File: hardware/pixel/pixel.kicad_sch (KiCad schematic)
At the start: 13 parts, among them J1 IN (male), J2 OUT (female), U1 WS2814F

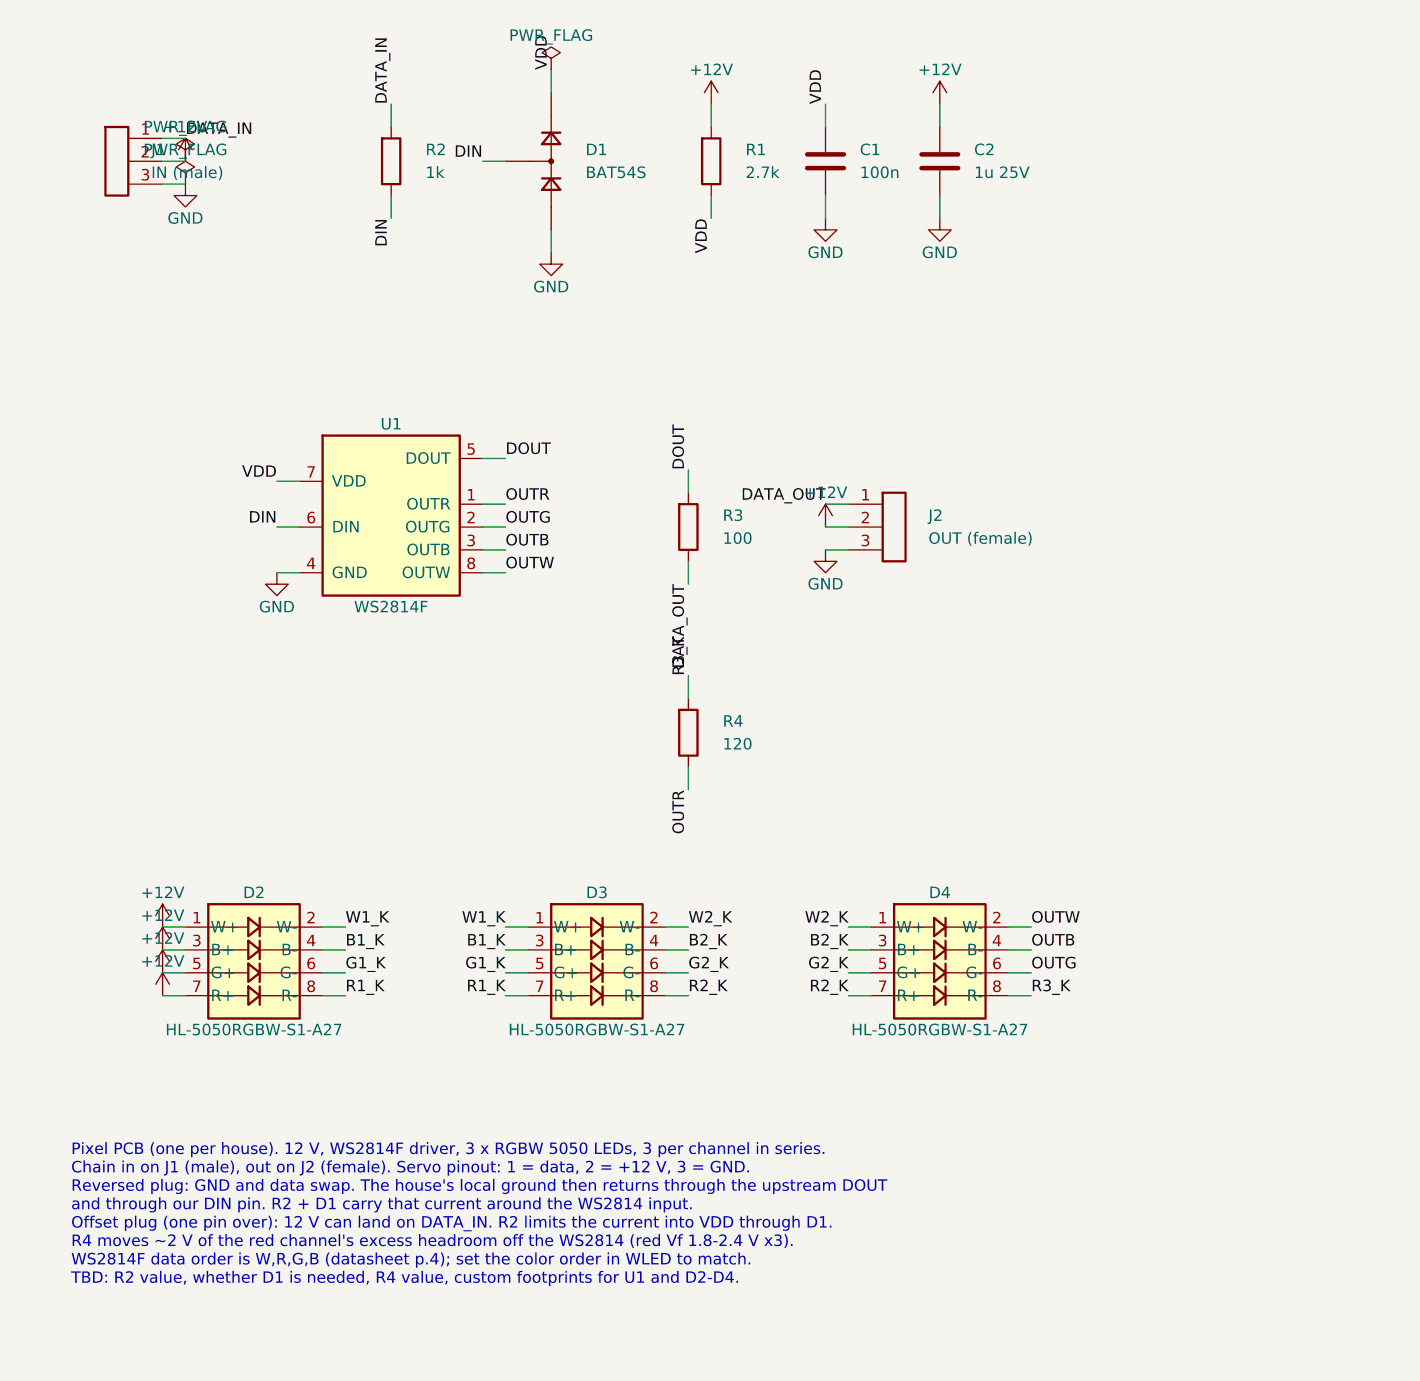
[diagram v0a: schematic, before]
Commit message: Pixel schematic: fix KiCad load error, use stock symbols, tidy layout
- Escape newlines in the notes text; KiCad 9.0.2 refused to load the file.
- Copy Device/Connector/power symbols verbatim from KiCad's stock libraries.
- Leave U1/LED footprints blank until the custom footprints exist.
- Rotate power symbols along their stubs, give PWR_FLAGs their own group,
  and space parts so labels don't overlap.

ERC in KiCad 9.0.2: 0 errors, 0 warnings. The kicad-cli netlist matches
the intended connectivity (20 nets).

Co-Authored-By: Claude Opus 5.5 <noreply@anthropic.com>
Claude-Session: https://claude.ai/code/session_01VgDz1r9wRYGVXFnVgHwR28
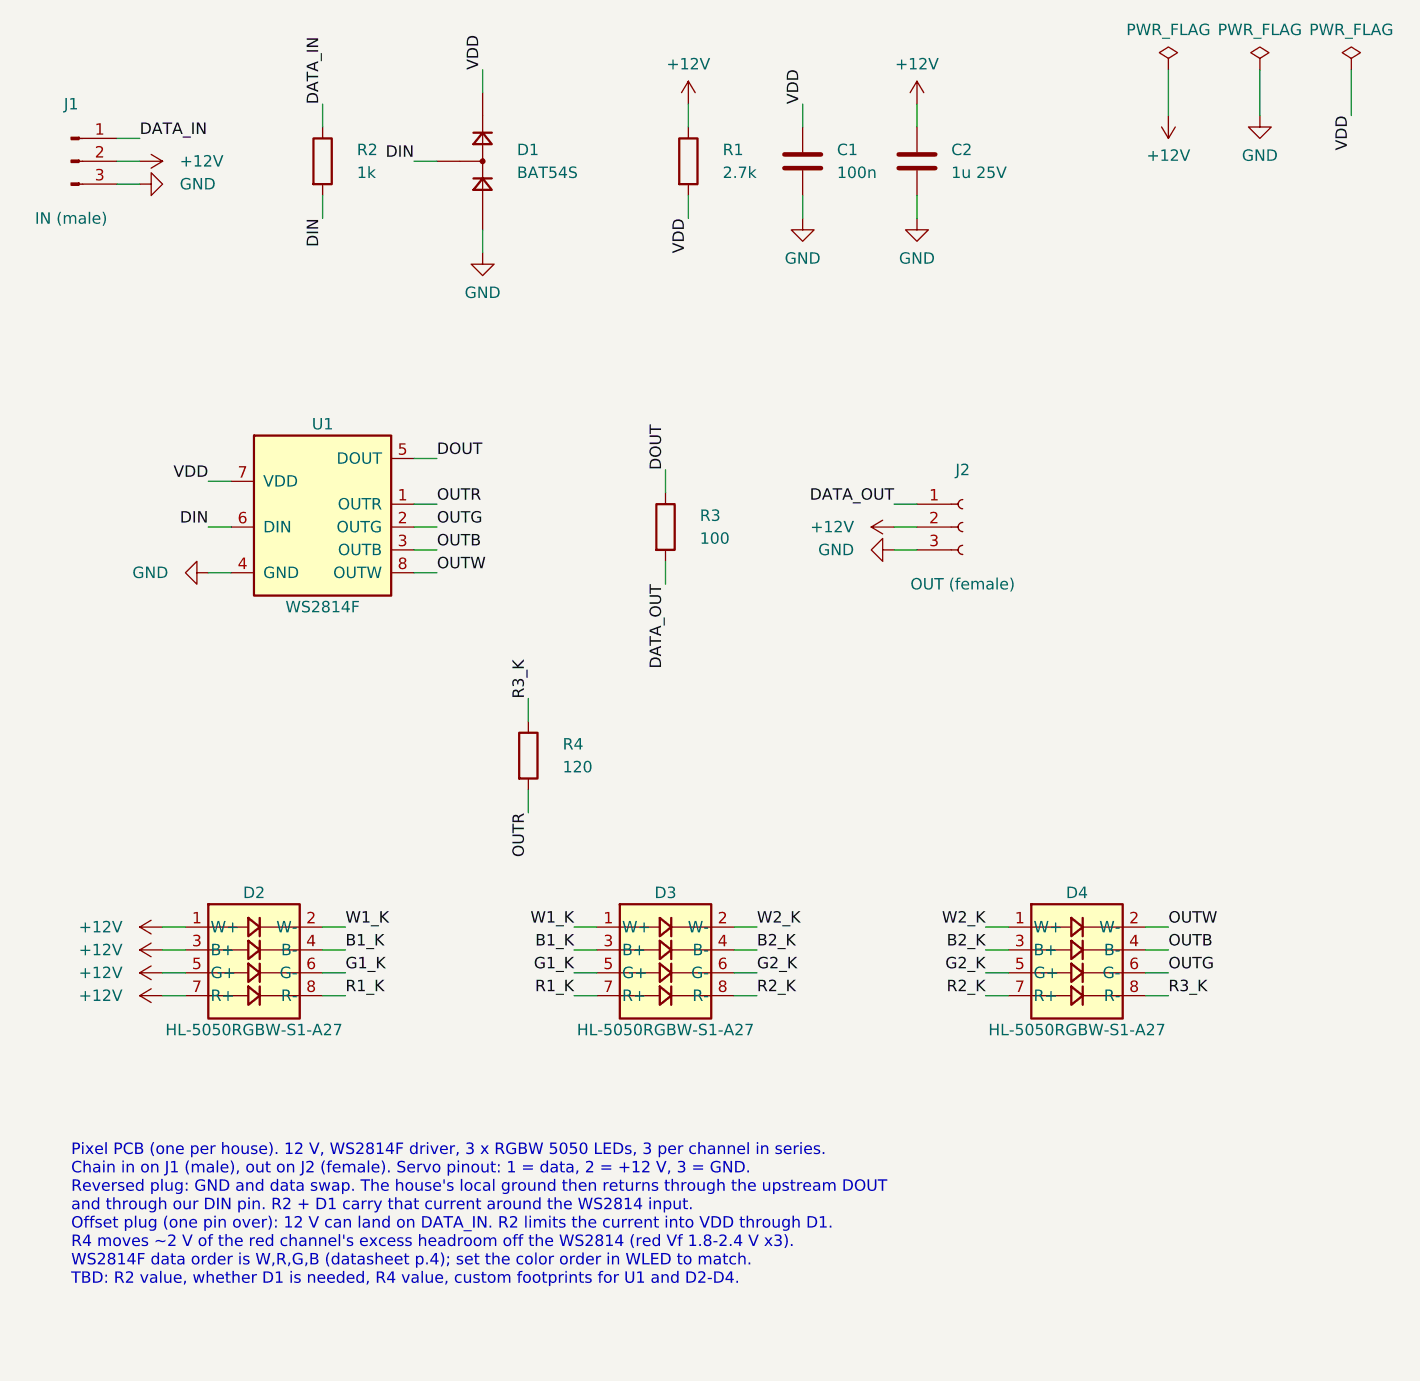
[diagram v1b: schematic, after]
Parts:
- D2, D3, D4: footprint village:LED_RGBW_5050-8P_HL -> (none)
- U1: footprint village:FSOP-8_2.85x3.25mm_P0.8mm -> (none)
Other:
- moved on the sheet: C1, C2, D1, D3, D4, R1, R2, R3, R4, U1

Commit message: Address review: fix reversed-plug analysis, add .gitignore, review nits
- Rewrite the reversed-plug explanation (README and sheet note): most of
  the return current flows through the upstream R3 into the upstream
  DOUT (10 mA min sink at 0.4 V), or into the Dig-Quad for the first
  house. R2/D1 carry only 1-2 mA.
- Fab-board test TBD now checks that the upstream DOUT/Dig-Quad output
  survives a reversal, and that VDD stays <= 5.3 V (abs max) with 12 V on
  DATA_IN.
- Cite the DIN input-voltage rating as the reason to keep D1.
- Note the Honglitronic spec sheet's "Under Development" status.
- C2: 1 uF 0402/25 V -> 1 uF 0603/50 V (C15849, basic) for DC bias.
- Rename the LED chain nets (RED1_K, WHT1_K, ...) so they don't read
  as resistor names.
- Target KiCad 10. Add .gitignore for KiCad local files.

ERC 0/0 in KiCad 9.0.2. Netlist diff against the previous revision:
identical pin groupings (20 nets), only the 9 net renames and C2's
value, footprint and part number changed.

Co-Authored-By: Claude Opus 5.5 <noreply@anthropic.com>
Claude-Session: https://claude.ai/code/session_01VgDz1r9wRYGVXFnVgHwR28
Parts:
- C2: value 1u 25V -> 1u 50V; footprint Capacitor_SMD:C_0402_1005Metric -> Capacitor_SMD:C_0603_1608Metric; LCSC C52923 -> C15849; MPN CL05A105KA5NQNC -> CL10A105KB8NNNC
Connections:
- net B1_K renamed BLU1_K
- net B2_K renamed BLU2_K
- net G1_K renamed GRN1_K
- net G2_K renamed GRN2_K
- net R1_K renamed RED1_K
- net R2_K renamed RED2_K
- net R3_K renamed RED3_K
- net W1_K renamed WHT1_K
- net W2_K renamed WHT2_K
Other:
- note added: "Pixel PCB (one per house). 12 V, WS2814F driver, 3 x RGBW 5050 LEDs, 3 per channel in series. Chain in on J1 (male), out on J2 (female). Servo pinout: 1 = data, 2 = +12 V, 3 = GND. Reversed plug: GND and data swap. This house's ground (and everything downstream) returns mostly through the upstream R3/DOUT (DOUT sink rated 10 mA min at 0.4 V). D1 clamps our DIN within the rails, and R2 limits the 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"
- note removed: "Pixel PCB (one per house). 12 V, WS2814F driver, 3 x RGBW 5050 LEDs, 3 per channel in series. Chain in on J1 (male), out on J2 (female). Servo pinout: 1 = data, 2 = +12 V, 3 = GND. Reversed plug: GND and data swap. The house's local ground then returns through the upstream DOUT and through our DIN pin. R2 + D1 carry that current around the WS2814 input. Offset plug (one pin over): 12 V can land o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"
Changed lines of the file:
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@@
 			(effects (font (size 1.27 1.27)) (justify left))
 		)
-		(property "Value" "1u 25V"
+		(property "Value" "1u 50V"
 			(at 123.19 52.07 0)
 			(effects (font (size 1.27 1.27)) (justify left))
 		)
-		(property "Footprint" "Capacitor_SMD:C_0402_1005Metric"
+		(property "Footprint" "Capacitor_SMD:C_0603_1608Metric"
 			(at 119.38 50.8 0)
 			(effects (font (size 1.27 1.27)) (hide yes))
@@
 			(effects (font (size 1.27 1.27)) (hide yes))
 		)
-		(property "Description" "12 V local bypass for LED PWM current"
+		(property "Description" "12 V local bypass for LED PWM current. 0603/50 V keeps more of its 1 uF at 12 V DC bias than 0402/25 V"
 			(at 119.38 50.8 0)
 			(effects (font (size 1.27 1.27)) (hide yes))
 		)
-		(property "LCSC" "C52923"
+		(property "LCSC" "C15849"
 			(at 119.38 50.8 0)
 			(effects (font (size 1.27 1.27)) (hide yes))
 		)
-		(property "MPN" "CL05A105KA5NQNC"
+		(property "MPN" "CL10A105KB8NNNC"
 			(at 119.38 50.8 0)
 			(effects (font (size 1.27 1.27)) (hide yes))
@@
 		(stroke (width 0) (type default))
 	)
-	(label "R3_K"
+	(label "RED3_K"
 		(at 76.2 110.49 90)
 		(effects (font (size 1.27 1.27)) (justify left bottom))
@@
 		(stroke (width 0) (type default))
 	)
-	(label "W1_K"
+	(label "WHT1_K"
 		(at 55.88 135.89 0)
 		(effects (font (size 1.27 1.27)) (justify left bottom))
@@
 		(stroke (width 0) (type default))
 	)
-	(label "B1_K"
+	(label "BLU1_K"
 		(at 55.88 138.43 0)
 		(effects (font (size 1.27 1.27)) (justify left bottom))
@@
 		(stroke (width 0) (type default))
 	)
-	(label "G1_K"
+	(label "GRN1_K"
 		(at 55.88 140.97 0)
 		(effects (font (size 1.27 1.27)) (justify left bottom))
@@
 		(stroke (width 0) (type default))
 	)
-	(label "R1_K"
+	(label "RED1_K"
 		(at 55.88 143.51 0)
 		(effects (font (size 1.27 1.27)) (justify left bottom))
@@
 		(stroke (width 0) (type default))
 	)
-	(label "W1_K"
+	(label "WHT1_K"
 		(at 81.28 135.89 180)
 		(effects (font (size 1.27 1.27)) (justify right bottom))
@@
 		(stroke (width 0) (type default))
 	)
-	(label "B1_K"
+	(label "BLU1_K"
 		(at 81.28 138.43 180)
 		(effects (font (size 1.27 1.27)) (justify right bottom))
@@
 		(stroke (width 0) (type default))
 	)
-	(label "G1_K"
+	(label "GRN1_K"
 		(at 81.28 140.97 180)
 		(effects (font (size 1.27 1.27)) (justify right bottom))
@@
 		(stroke (width 0) (type default))
 	)
-	(label "R1_K"
+	(label "RED1_K"
 		(at 81.28 143.51 180)
 		(effects (font (size 1.27 1.27)) (justify right bottom))
@@
 		(stroke (width 0) (type default))
 	)
-	(label "W2_K"
+	(label "WHT2_K"
 		(at 101.6 135.89 0)
 		(effects (font (size 1.27 1.27)) (justify left bottom))
@@
 		(stroke (width 0) (type default))
 	)
-	(label "B2_K"
+	(label "BLU2_K"
 		(at 101.6 138.43 0)
 		(effects (font (size 1.27 1.27)) (justify left bottom))
@@
 		(stroke (width 0) (type default))
 	)
-	(label "G2_K"
+	(label "GRN2_K"
 		(at 101.6 140.97 0)
 		(effects (font (size 1.27 1.27)) (justify left bottom))
@@
 		(stroke (width 0) (type default))
 	)
-	(label "R2_K"
+	(label "RED2_K"
 		(at 101.6 143.51 0)
 		(effects (font (size 1.27 1.27)) (justify left bottom))
@@
 		(stroke (width 0) (type default))
 	)
-	(label "W2_K"
+	(label "WHT2_K"
 		(at 127 135.89 180)
 		(effects (font (size 1.27 1.27)) (justify right bottom))
@@
 		(stroke (width 0) (type default))
 	)
-	(label "B2_K"
+	(label "BLU2_K"
 		(at 127 138.43 180)
 		(effects (font (size 1.27 1.27)) (justify right bottom))
@@
 		(stroke (width 0) (type default))
 	)
-	(label "G2_K"
+	(label "GRN2_K"
 		(at 127 140.97 180)
 		(effects (font (size 1.27 1.27)) (justify right bottom))
@@
 		(stroke (width 0) (type default))
 	)
-	(label "R2_K"
+	(label "RED2_K"
 		(at 127 143.51 180)
 		(effects (font (size 1.27 1.27)) (justify right bottom))
@@
 		(stroke (width 0) (type default))
 	)
-	(label "R3_K"
+	(label "RED3_K"
 		(at 147.32 143.51 0)
 		(effects (font (size 1.27 1.27)) (justify left bottom))
@@
 		(effects (font (size 1.27 1.27)) (justify right bottom))
 	)
-	(text "Pixel PCB (one per house). 12 V, WS2814F driver, 3 x RGBW 5050 LEDs, 3 per channel in series.\nChain in on J1 (male), out on J2 (female). Servo pinout: 1 = data, 2 = +12 V, 3 = GND.\nReversed plug: GND and data swap. The house's local ground then returns through the upstream DOUT\nand through our DIN pin. R2 + D1 carry that current around the WS2814 input.\nOffset plug (one pin over): 12 V can land on DATA_IN. R2 limits the current into VDD through D1.\nR4 moves ~2 V of the red channel's excess headroom off the WS2814 (red Vf 1.8-2.4 V x3).\nWS2814F data order is W,R,G,B (datasheet p.4); set the color order in WLED to match.\nTBD: R2 value, whether D1 is needed, R4 value, custom footprints for U1 and D2-D4."
+	(text "Pixel PCB (one per house). 12 V, WS2814F driver, 3 x RGBW 5050 LEDs, 3 per channel in series.\nChain in on J1 (male), out on J2 (female). Servo pinout: 1 = data, 2 = +12 V, 3 = GND.\nReversed plug: GND and data swap. This house's ground (and everything downstream) returns mostly\nthrough the upstream R3/DOUT (DOUT sink rated 10 mA min at 0.4 V). D1 clamps our DIN within the rails,\nand R2 limits the current through D1.\nOffset plug (one pin over): 12 V can land on DATA_IN. R2 limits the current into VDD through D1\n(~7 mA); VDD must stay under its 5.3 V absolute max.\nR4 moves ~2 V of the red channel's excess headroom off the WS2814 (red Vf 1.8-2.4 V x3).\nWS2814F data order is W,R,G,B (datasheet p.4); set the color order in WLED to match.\nTBD: R2 value, R4 value, custom footprints for U1 and D2-D4. Fab-board tests: reversed plug\n(upstream DOUT / Dig-Quad output survive), offset plug (VDD <= 5.3 V)."
 		(exclude_from_sim no)
 		(at 25.4 160.02 0)

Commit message: Pixel PCB: assign custom footprints to U1 and D2-D4
Co-Authored-By: Claude Opus 5.5 <noreply@anthropic.com>
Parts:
- D2, D3, D4: footprint (none) -> village:LED_Honglitronic_HL-5050RGBW_5.0x5.0mm_P1.2mm
- U1: footprint (none) -> village:FSOP-8_1.65x3.25mm_P0.8mm
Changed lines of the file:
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@@
 			(effects (font (size 1.27 1.27)))
 		)
-		(property "Footprint" ""
+		(property "Footprint" "village:FSOP-8_1.65x3.25mm_P0.8mm"
 			(at 53.34 91.44 0)
 			(effects (font (size 1.27 1.27)) (hide yes))
@@
 			(effects (font (size 1.27 1.27)))
 		)
-		(property "Footprint" ""
+		(property "Footprint" "village:LED_Honglitronic_HL-5050RGBW_5.0x5.0mm_P1.2mm"
 			(at 45.72 139.7 0)
 			(effects (font (size 1.27 1.27)) (hide yes))
@@
 			(effects (font (size 1.27 1.27)))
 		)
-		(property "Footprint" ""
+		(property "Footprint" "village:LED_Honglitronic_HL-5050RGBW_5.0x5.0mm_P1.2mm"
 			(at 91.44 139.7 0)
 			(effects (font (size 1.27 1.27)) (hide yes))
@@
 			(effects (font (size 1.27 1.27)))
 		)
-		(property "Footprint" ""
+		(property "Footprint" "village:LED_Honglitronic_HL-5050RGBW_5.0x5.0mm_P1.2mm"
 			(at 137.16 139.7 0)
 			(effects (font (size 1.27 1.27)) (hide yes))

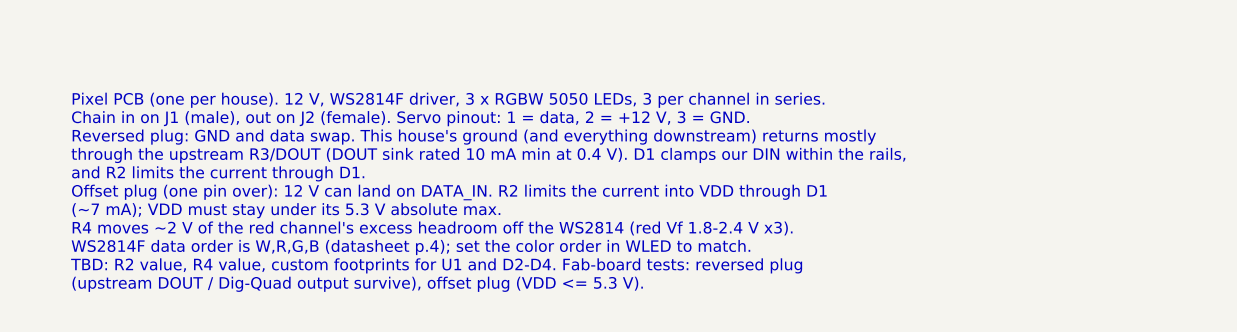
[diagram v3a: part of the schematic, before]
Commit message: Pixel PCB: silkscreen markings for plugging in and JLCPCB assembly review
Bottom: pin-1 (data) triangles and +/- marks at each header (shapes, so
they read correctly on the back), and a JLCJLCJLCJLC order-number
placeholder. Top: revision v0.1, and a pin-1 dot inside U1 because J1's
pad clips the footprint's own pin-1 line. The schematic note no
longer lists the footprints as TBD. DRC: 0 errors; ERC clean.

Co-Authored-By: Claude Opus 5.5 <noreply@anthropic.com>
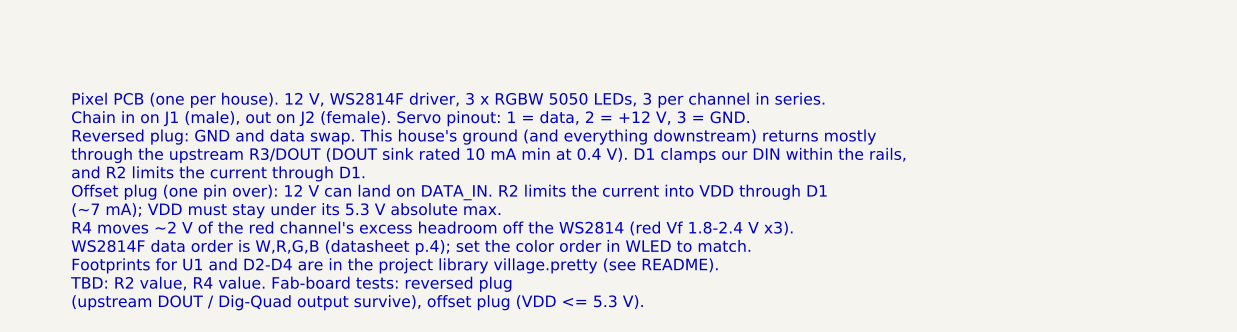
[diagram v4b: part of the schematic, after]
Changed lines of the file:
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@@
 		(comment 1 "Draft v0.1: ERC clean in KiCad 9.0.2")
 	)
+  (text "Pixel PCB (one per house). 12 V, WS2814F driver, 3 x RGBW 5050 LEDs, 3 per channel in series.\nChain in on J1 (male), out on J2 (female). Servo pinout: 1 = data, 2 = +12 V, 3 = GND.\nReversed plug: GND and data swap. This house's ground (and everything downstream) returns mostly\nthrough the upstream R3/DOUT (DOUT sink rated 10 mA min at 0.4 V). D1 clamps our DIN within the rails,\nand R2 limits the current through D1.\nOffset plug (one pin over): 12 V can land on DATA_IN. R2 limits the current into VDD through D1\n(~7 mA); VDD must stay under its 5.3 V absolute max.\nR4 moves ~2 V of the red channel's excess headroom off the WS2814 (red Vf 1.8-2.4 V x3).\nWS2814F data order is W,R,G,B (datasheet p.4); set the color order in WLED to match.\nFootprints for U1 and D2-D4 are in the project library village.pretty (see README).\nTBD: R2 value, R4 value. Fab-board tests: reversed plug\n(upstream DOUT / Dig-Quad output survive), offset plug (VDD <= 5.3 V)."
+    (at 25.4 160.02 0)
+    (effects (font (size 1.27 1.27)) (justify left top))
+  )
 	(symbol
 		(lib_id "Connector:Conn_01x03_Pin")
@@
 		(effects (font (size 1.27 1.27)) (justify right bottom))
 	)
-	(text "Pixel PCB (one per house). 12 V, WS2814F driver, 3 x RGBW 5050 LEDs, 3 per channel in series.\nChain in on J1 (male), out on J2 (female). Servo pinout: 1 = data, 2 = +12 V, 3 = GND.\nReversed plug: GND and data swap. This house's ground (and everything downstream) returns mostly\nthrough the upstream R3/DOUT (DOUT sink rated 10 mA min at 0.4 V). D1 clamps our DIN within the rails,\nand R2 limits the current through D1.\nOffset plug (one pin over): 12 V can land on DATA_IN. R2 limits the current into VDD through D1\n(~7 mA); VDD must stay under its 5.3 V absolute max.\nR4 moves ~2 V of the red channel's excess headroom off the WS2814 (red Vf 1.8-2.4 V x3).\nWS2814F data order is W,R,G,B (datasheet p.4); set the color order in WLED to match.\nTBD: R2 value, R4 value, custom footprints for U1 and D2-D4. Fab-board tests: reversed plug\n(upstream DOUT / Dig-Quad output survive), offset plug (VDD <= 5.3 V)."
-		(exclude_from_sim no)
-		(at 25.4 160.02 0)
-		(effects (font (size 1.27 1.27)) (justify left top))
-	)
 	(sheet_instances
